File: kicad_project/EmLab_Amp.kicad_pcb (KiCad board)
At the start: 4 copper layers, 164 parts, among them J1 JTAG, J2 USB_C_Receptacle, J3 GPIO_EXP, J4 BNC, U1 TPS7A80, U10 THS4131ID, U11 THS4131ID, U12 THS4131ID, U2 LT3094xDD, U3 LT3045xDD, U4 TPS6513x, U5 LPC4370-TFBGA100, U6 IS25LP080D, U7 ADR421, U8 MCP601R, U9 LMH6518, Y1 12MHz Crystal

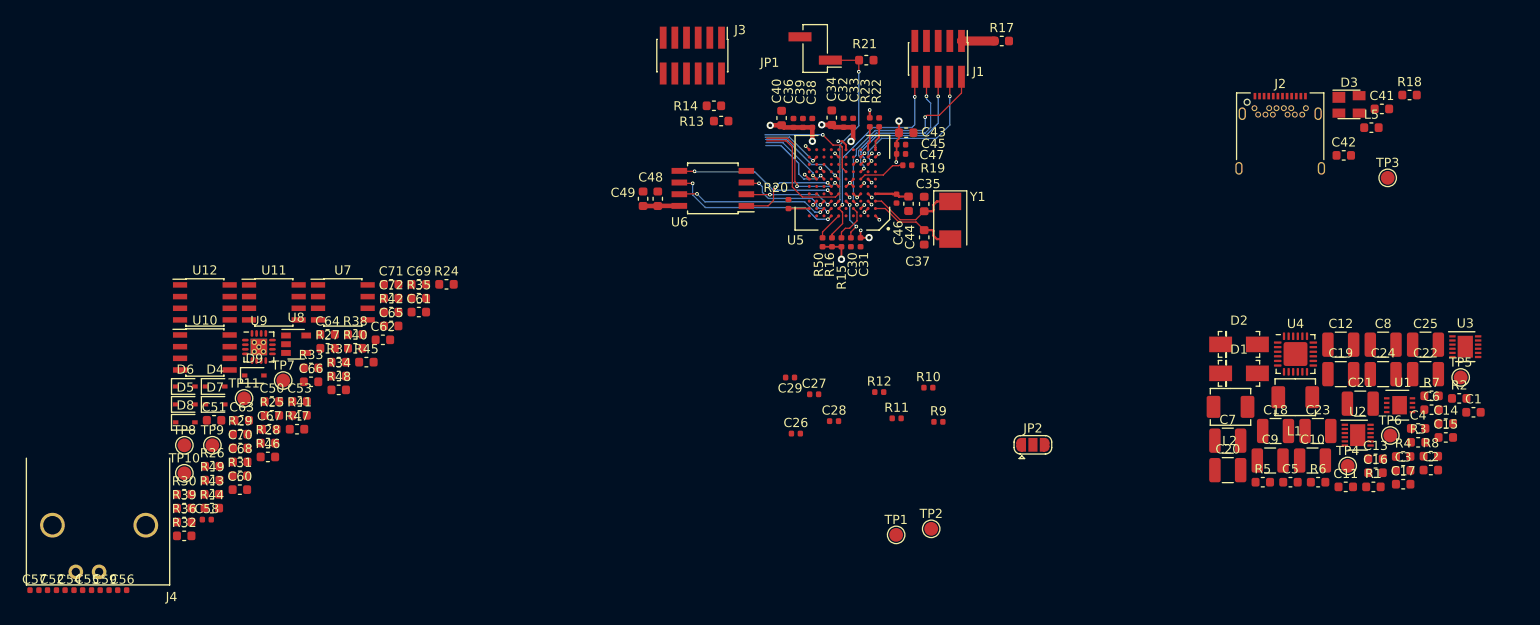
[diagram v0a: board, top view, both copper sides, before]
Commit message: PCB: Amplifier done, digital done
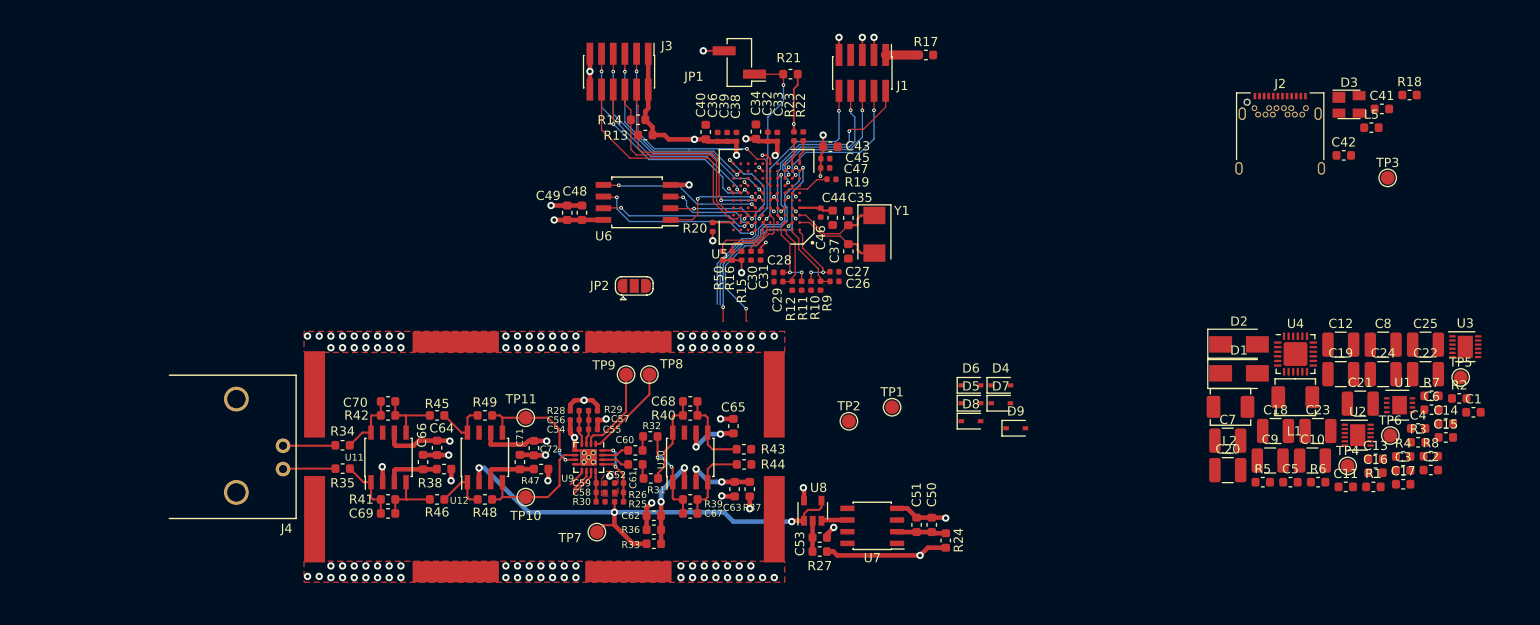
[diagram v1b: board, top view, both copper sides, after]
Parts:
- added REF**: Shield_clip_Sx711, LoaDy:Shield_clip_Sx711, F.Cu at (112.6, 116.3)
- added REF**: Shield_clip_Sx711, LoaDy:Shield_clip_Sx711, F.Cu at (131.4, 116.3)
- added REF**: Shield_clip_Sx711, LoaDy:Shield_clip_Sx711, F.Cu at (112.6, 91.3)
- added REF**: Shield_clip_Sx711, LoaDy:Shield_clip_Sx711, F.Cu at (131.4, 91.3)
- added REF**: Shield_clip_Sx711, LoaDy:Shield_clip_Sx711, F.Cu at (147.3, 110.6)
- added REF**: Shield_clip_Sx711, LoaDy:Shield_clip_Sx711, F.Cu at (147.3, 97.0)
- added REF**: Shield_clip_Sx711, LoaDy:Shield_clip_Sx711, F.Cu at (97.3, 110.6)
- added REF**: Shield_clip_Sx711, LoaDy:Shield_clip_Sx711, F.Cu at (97.3, 97.0)
- D1, D2: footprint LoaDy:DO-214AC -> Diode_SMD:D_SMA
- R25, R26, R28, R29, R30: footprint Resistor_SMD:R_0603_1608Metric -> Resistor_SMD:R_0402_1005Metric
- moved D4 85.5 mm to (172.0, 96.0)
- moved D5 85.5 mm to (168.7, 98.0)
- moved D6 85.5 mm to (168.7, 96.0)
- moved D7 85.5 mm to (172.0, 98.0)
- moved D8 85.5 mm to (168.7, 99.9)
- moved D9 83.1 mm to (173.6, 100.7)
- moved C51 77.3 mm to (162.8, 111.2), turned to 270 degrees
- moved C50 73.1 mm to (164.5, 111.2), turned to 270 degrees
- moved C57 63.6 mm to (127.6, 99.8), turned to 180 degrees
- moved C52 62.8 mm to (130.4, 106.7)
- moved U7 62.5 mm to (158.0, 111.3), turned to 180 degrees
- moved R24 61.1 mm to (166.0, 112.9), turned to 90 degrees
- moved U8 59.1 mm to (151.5, 109.7), turned to 90 degrees
- moved C53 58.5 mm to (152.3, 112.6), turned to 180 degrees
- moved R44 58.1 mm to (144.0, 104.6)
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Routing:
- net GND: track 5.06 -> 59.9 mm, vias 8 -> 120
- net /Amplifier/V_REF: track 0.00 -> 52.2 mm, vias 0 -> 3
- net /LPC4370-GPIO/GPIO_5: track 0.57 -> 26.2 mm, vias 1 -> 0
- net /LPC4370-GPIO/SSP1_MISO: track 0.53 -> 24.0 mm, vias 1 -> 2
- net /Amplifier/S3_CS: track 0.57 -> 23.0 mm
- net /LPC4370-GPIO/SSP1_MOSI: track 0.59 -> 22.9 mm, vias 1 -> 2
- net /Amplifier/S3_SCLK: track 0.57 -> 22.9 mm
- net +5V: track 0.00 -> 22.0 mm, vias 0 -> 5
- net -5V: track 0.00 -> 21.4 mm, vias 0 -> 4
- net +3V3: track 53.9 -> 75.3 mm
- net /LPC4370-GPIO/GPIO_3: track 7.34 -> 25.0 mm, vias 1 -> 2
- net /LPC4370-GPIO/GPIO_2: track 9.74 -> 26.4 mm, vias 1 -> 2
- net /LPC4370-GPIO/GPIO_1: track 6.84 -> 22.6 mm, vias 1 -> 2
- net /LPC4370-GPIO/GPIO_0: track 11.9 -> 26.8 mm, vias 1 -> 2
- net /Amplifier/STAGE2_POS: track 0.00 -> 14.3 mm
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- added copper zone on F.Cu, net GND

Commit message: PCB: finished analog and digital
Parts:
- removed the REF** at (112.6, 116.3)
- removed the REF** at (131.4, 116.3)
- removed the REF** at (112.6, 91.3)
- removed the REF** at (147.3, 110.6)
- removed the REF** at (147.3, 97.0)
- removed the REF** at (97.3, 110.6)
- removed the REF** at (97.3, 97.0)
- added R51: 1M, Resistor_SMD:R_0603_1608Metric, F.Cu at (195.1, 65.8)
- added R52: 1M, Resistor_SMD:R_0603_1608Metric, F.Cu at (195.1, 64.3)
- added REF**: Shield_clip_Sx711, LoaDy:Shield_clip_Sx711, F.Cu at (147.3, 110.7)
- added REF**: Shield_clip_Sx711, LoaDy:Shield_clip_Sx711, F.Cu at (147.3, 96.9)
- added REF**: Shield_clip_Sx711, LoaDy:Shield_clip_Sx711, F.Cu at (97.3, 96.9)
- added REF**: Shield_clip_Sx711, LoaDy:Shield_clip_Sx711, F.Cu at (97.3, 110.7)
- added REF**: Shield_clip_Sx711, LoaDy:Shield_clip_Sx711, F.Cu at (131.3, 116.3)
- added REF**: Shield_clip_Sx711, LoaDy:Shield_clip_Sx711, F.Cu at (112.4, 116.3)
- added REF**: Shield_clip_Sx711, LoaDy:Shield_clip_Sx711, F.Cu at (112.5, 91.3)
- moved TP5 56.9 mm to (168.0, 113.0)
- moved C1 54.5 mm to (169.4, 106.2)
- moved U3 53.2 mm to (172.3, 109.5)
- moved TP4 52.6 mm to (178.6, 62.5)
- moved U1 50.7 mm to (175.6, 66.7)
- moved C2 49.8 mm to (171.1, 91.1)
- moved R2 49.8 mm to (172.8, 105.9)
- moved C8 49.1 mm to (167.9, 109.5)
- moved C4 49.0 mm to (178.5, 71.0)
- moved TP6 49.0 mm to (165.5, 98.7)
- moved C6 48.2 mm to (172.7, 112.6)
- moved C3 47.9 mm to (182.7, 70.7)
- moved R1 40.3 mm to (173.1, 98.9)
- moved C7 38.5 mm to (181.6, 66.7)
- moved U2 38.1 mm to (173.3, 95.3)
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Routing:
- net /Amplifier/S3_SCLK: track 22.9 -> 59.0 mm, vias 1 -> 2
- net /Amplifier/S3_CS: track 23.0 -> 58.6 mm, vias 1 -> 2
- net /Amplifier/S3_DIO: track 2.54 -> 35.8 mm, vias 0 -> 2
- net /LPC4370-JTAG-PWR-MISC/ADC0: track 0.00 -> 24.6 mm
- net /LPC4370-JTAG-PWR-MISC/ADC3: track 0.00 -> 20.5 mm
- net +5V: track 22.0 -> 11.0 mm, vias 5 -> 6
- net GND: track 59.9 -> 69.2 mm, vias 120 -> 140
- net /LPC4370-GPIO/SSP1_MOSI: track 22.9 -> 25.8 mm
- net +3V3: track 75.3 -> 77.5 mm, vias 15 -> 17
- net /Amplifier/V_REF: track 52.2 -> 54.2 mm
- net Net-(D7-Pad2): track 0.00 -> 1.94 mm
- net Net-(D4-Pad2): track 0.00 -> 1.91 mm
- net Net-(U7-Pad6): track 2.86 -> 4.61 mm
- net /LPC4370-GPIO/SSP1_MISO: track 24.0 -> 25.7 mm
- net -5V: track 21.4 -> 22.8 mm, vias 4 -> 5
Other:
- board outline added: 147.2 x 58 mm

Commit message: PCB layout done
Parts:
- C8, C9: footprint Capacitor_SMD:C_1210_3225Metric -> LoaDy:C_1210_3225Metric_SPLIT
- U3: footprint Package_DFN_QFN:DFN-12-1EP_3x3mm_P0.45mm_EP1.66x2.38mm -> Package_DFN_QFN:DFN-10-1EP_3x3mm_P0.5mm_EP1.55x2.48mm
- moved C22 45.0 mm to (177.8, 96.6), turned to 90 degrees
- moved C23 44.2 mm to (184.0, 115.2), turned to 270 degrees
- moved R18 44.1 mm to (177.0, 84.1)
- moved C20 43.6 mm to (177.8, 101.3), turned to 270 degrees
- moved C15 42.0 mm to (180.6, 106.8), turned to 270 degrees
- moved C24 41.4 mm to (174.6, 96.6), turned to 90 degrees
- moved C25 40.0 mm to (180.8, 115.2), turned to 270 degrees
- moved C17 38.2 mm to (185.0, 110.8), turned to 90 degrees
- moved C18 36.6 mm to (174.6, 101.3), turned to 270 degrees
- moved C41 35.0 mm to (184.0, 84.8), turned to 270 degrees
- moved L5 34.6 mm to (181.6, 84.1)
- moved R7 33.2 mm to (186.4, 110.8), turned to 90 degrees
- moved C42 33.0 mm to (179.3, 84.8), turned to 270 degrees
- moved C14 32.5 mm to (182.1, 106.7), turned to 270 degrees
- moved C19 30.9 mm to (180.8, 110.6), turned to 90 degrees
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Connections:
- net /LPC4370-USB/USB0_D+ renamed Net-(D3-Pad3)
- net /LPC4370-USB/USB0_D- renamed Net-(D3-Pad2)
- U4 pad 25: (no net) -> GND
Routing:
- net +3V3: track 77.5 -> 168.4 mm, vias 17 -> 25
- net Net-(D3-Pad2): track 0.00 -> 42.2 mm
- net Net-(D3-Pad3): track 0.00 -> 41.4 mm, vias 0 -> 1
- net Net-(R18-Pad1): track 0.53 -> 29.0 mm, vias 1 -> 3
- net /LPC4370-USB/USB_VBUS: track 0.00 -> 15.7 mm, vias 0 -> 20
- net Net-(C11-Pad1): track 0.00 -> 12.6 mm, vias 0 -> 2
- net /Power/VPOS: track 0.00 -> 10.9 mm, vias 0 -> 2
- net GND: track 69.2 -> 79.8 mm, vias 140 -> 239
- net /Power/VNEG: track 0.00 -> 10.1 mm
- net Net-(C17-Pad2): track 0.00 -> 6.33 mm
- net Net-(C15-Pad1): track 0.00 -> 5.80 mm
- net Net-(C16-Pad1): track 0.00 -> 4.81 mm
- net +5V: track 11.0 -> 15.6 mm, vias 6 -> 12
- net Net-(C14-Pad1): track 0.00 -> 3.50 mm
- net Net-(C42-Pad1): track 0.00 -> 3.09 mm
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- added copper zone on F.Cu, net +3V3
- added copper zone on In2.Cu, net +3V3
- added copper zone on F.Cu, net +5V
- added copper zone on In2.Cu, net +5V
- added copper zone on F.Cu, net -5V
- added copper zone on In2.Cu, net -5V
- added copper zone on F.Cu, net /LPC4370-USB/USB_VBUS
- added copper zone on In2.Cu, net /LPC4370-USB/USB_VBUS
- added copper zone on F.Cu, net /Power/VNEG
- added copper zone on F.Cu, net /Power/VPOS
- added copper zone on In1.Cu, net GND
- added copper zone on F.Cu, net Net-(C5-Pad2)
- added copper zone on F.Cu, net Net-(C6-Pad2)
- added copper zone on F.Cu, net Net-(D1-Pad2)
- added copper zone on F.Cu, net Net-(D2-Pad1)
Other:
- board size 147.2 x 58 mm -> 118.1 x 58 mm

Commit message: PCB rev. 1 done
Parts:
- added G***: LOGO, LoaDy:FI_LOGO_11x10mm, F.Cu at (93.3, 72.5)
- added REF**: MountingHole_3.2mm_M3, MountingHole:MountingHole_3.2mm_M3, F.Cu at (85.3, 114.7)
- added REF**: MountingHole_3.2mm_M3, MountingHole:MountingHole_3.2mm_M3, F.Cu at (85.3, 64.5)
- added REF**: MountingHole_3.2mm_M3, MountingHole:MountingHole_3.2mm_M3, F.Cu at (195.6, 114.7)
- added REF**: MountingHole_3.2mm_M3, MountingHole:MountingHole_3.2mm_M3, F.Cu at (195.6, 64.5)
- moved R51 0.30 mm to (178.5, 76.7)
- moved R52 0.29 mm to (178.5, 79.5)
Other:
- board text added: "1"
- board text added: "1: OUT+ 2: OUT- 3: VBUS 4: 3V3 5: 5V 6: -5V 7: VREF 8: STAGE3+ 9: STAGE3- 10: STAGE2+ 11: STAGE2-"
- board text added: "3V3 I2C_SDA I2C_SCL P6_9 P6_11 GND"
- board text added: "3V3 P6_1 P6_2 P6_4 P6_5 GND"
- board text added: "3V3_TARGET GND GND NC GND"
- board text added: "80dB Amp + Digitizer Rev. 1 Oldřich Pecák FI MUNI, May 2019"
- board text added: "BOOT"
- board text added: "GPIO"
- board text added: "JTAG"
- board text added: "MISO"
- board text added: "MOSI"
- board text added: "OPEN - SPIFI CLOSED - DFU"
- board text added: "TMS TCK TDO TDI RESET"
- board text added: "TP"
